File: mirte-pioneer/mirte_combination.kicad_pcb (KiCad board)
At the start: 2 copper layers, 55 x 81.9 mm, 48 parts, among them J1 Servo3, J10 IR1, J11 Conn_01x13_Female, J12 IR Object Detector 1, J14 IR2, J17 MC1, J18 MC2, J19 Servo1, J2 Conn_01x20_Female, J20 SRF1, J21 ENC2, J23 MC1-A, J24 MC1-B, J25 SRF2, J26 ENC1, J27 Servo2, J28 I2C2, J3 Servo4, J30 I2C1, J33 line out left, J34 Power in, J35 Power out, J37 on/off, J4 Conn_01x20_Female, J7 Keypad, J8 Conn_01x06_Female, J9 IR Object Detector 2, Q1 DMG2305UX, Q2 DMN2050L, SW1 on/off, U1 CH340C, U2 CH340E

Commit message: Fix logo reference name
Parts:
- renumbered G*** to G1, G*** to G2
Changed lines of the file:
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@@
     (at 112.5 58.575 -90)
     (attr board_only exclude_from_pos_files exclude_from_bom)
-    (fp_text reference "G***" (at -1.285 0.39 180) (layer "F.Fab")
+    (fp_text reference "G1" (at -1.285 0.39 180) (layer "F.Fab")
         (effects (font (size 1.524 1.524) (thickness 0.3)))
     )
@@
     (at 104.275 114.325 -90)
     (attr board_only exclude_from_pos_files exclude_from_bom)
-    (fp_text reference "G***" (at 0.425 0.75 90) (layer "F.Fab")
+    (fp_text reference "G2" (at 0.425 0.75 90) (layer "F.Fab")
         (effects (font (size 1.524 1.524) (thickness 0.3)))
     )

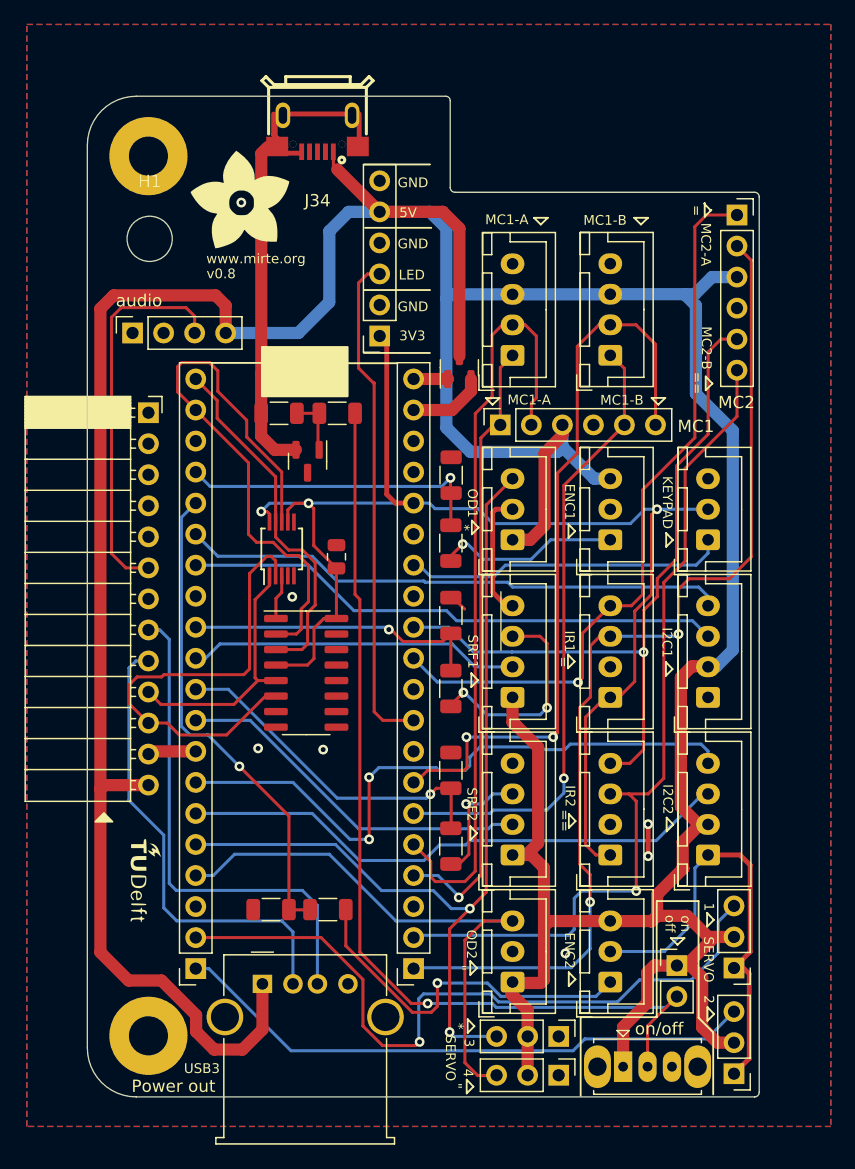
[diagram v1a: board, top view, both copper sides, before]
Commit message: Fix text unreadable servo 1&2 by move edge
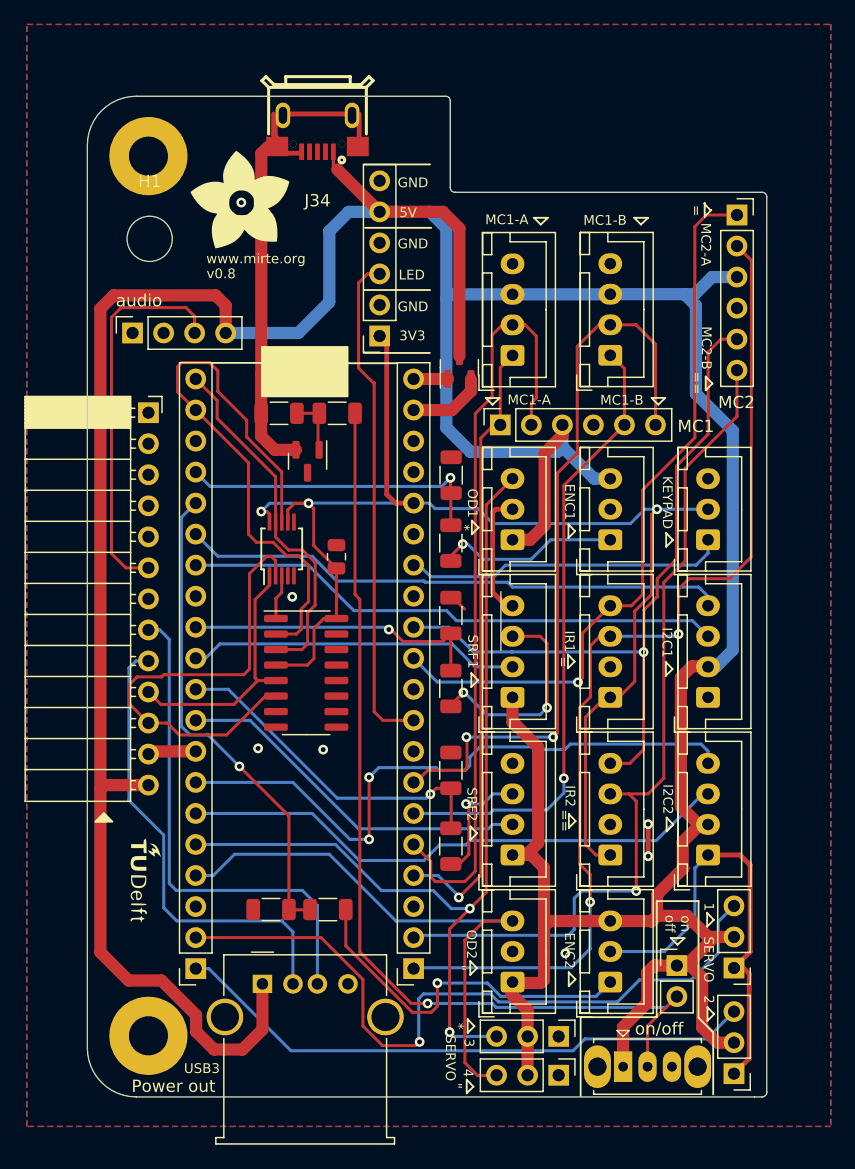
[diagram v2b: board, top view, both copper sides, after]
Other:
- board size 55 x 81.9 mm -> 55.6 x 81.9 mm
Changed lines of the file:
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@@
   (gr_line (start 104 50.1) (end 129.337 50.100408)
     (stroke (width 0.1) (type solid)) (layer "Edge.Cuts"))
-  (gr_arc (start 154.61 57.959) (mid 154.879408 58.070592) (end 154.991 58.34)
+  (gr_arc (start 155.230592 57.959) (mid 155.5 58.070592) (end 155.611592 58.34)
     (stroke (width 0.1) (type solid)) (layer "Edge.Cuts"))
   (gr_line (start 129.702592 50.466) (end 129.7 57.578)
     (stroke (width 0.1) (type solid)) (layer "Edge.Cuts"))
-  (gr_line (start 154.991 58.34) (end 154.991 131.619)
+  (gr_line (start 130.099 57.959) (end 155.230592 57.959)
+    (stroke (width 0.1) (type default)) (layer "Edge.Cuts"))
+  (gr_line (start 155.611592 58.34) (end 155.611592 131.619)
     (stroke (width 0.1) (type solid)) (layer "Edge.Cuts"))
-  (gr_arc (start 154.991 131.619) (mid 154.879408 131.888408) (end 154.61 132)
+  (gr_arc (start 155.611592 131.619) (mid 155.5 131.888408) (end 155.230592 132)
     (stroke (width 0.1) (type solid)) (layer "Edge.Cuts"))
   (gr_arc (start 129.337 50.100408) (mid 129.595513 50.207487) (end 129.702592 50.466)
     (stroke (width 0.1) (type solid)) (layer "Edge.Cuts"))
+  (gr_line (start 155.230592 132) (end 154.61 132)
+    (stroke (width 0.1) (type default)) (layer "Edge.Cuts"))
   (gr_line (start 100 128) (end 100 54.1)
     (stroke (width 0.1) (type solid)) (layer "Edge.Cuts"))
-  (gr_line (start 154.61 57.959) (end 130.099 57.959)
-    (stroke (width 0.1) (type solid)) (layer "Edge.Cuts"))
   (gr_arc (start 130.099 57.959) (mid 129.820592 57.851136) (end 129.7 57.578)

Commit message: Change obj detector to 5V, add header for usb (lego)
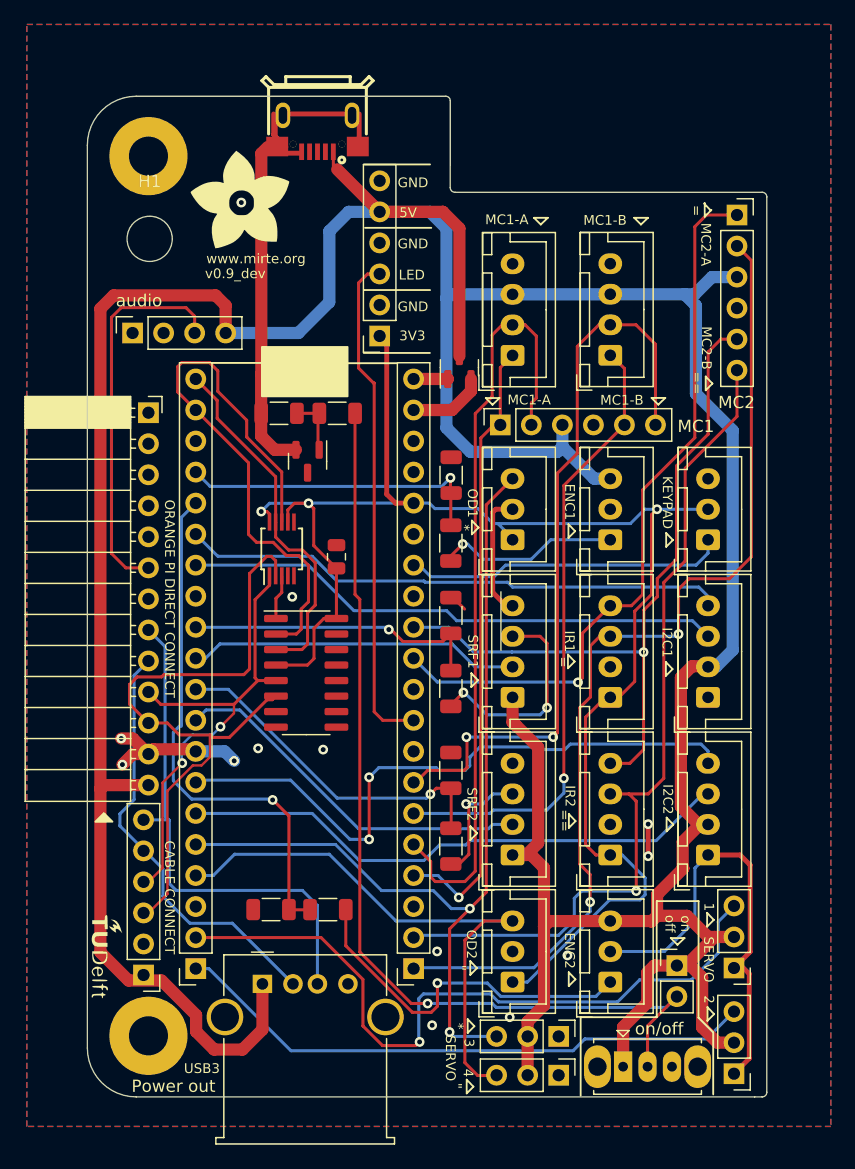
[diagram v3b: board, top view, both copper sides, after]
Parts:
- added J5: Conn_01x06_Pin, Connector_PinHeader_2.54mm:PinHeader_1x06_P2.54mm_Vertical, F.Cu at (104.6, 122.0)
- moved G2 6.99 mm to (101.1, 120.5)
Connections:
- J12 pad 1: 5V -> 3V3
- J9 pad 1: 5V -> 3V3
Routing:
- net 3V3: track 109.4 -> 130.0 mm
- net D+: track 20.8 -> 40.4 mm, vias 0 -> 2
- net D-: track 38.2 -> 56.6 mm
- net 5V: track 351.1 -> 336.6 mm
- net D_GND: track 60.3 -> 69.2 mm, vias 7 -> 13
- net GP3: track 40.0 -> 43.7 mm
- net usb-dp3: track 41.3 -> 43.6 mm
- net usb-dm3: track 38.3 -> 36.5 mm
- net GP16: track 84.9 -> 83.1 mm
- net GP9: track 29.7 -> 30.5 mm
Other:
- board text added: "CABLE CONNECT"
- board text added: "ORANGE PI DIRECT CONNECT"
- board text added: "v0.9_dev"
- board text removed: "v0.8"

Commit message: update version8, uart, usb c, usb switch
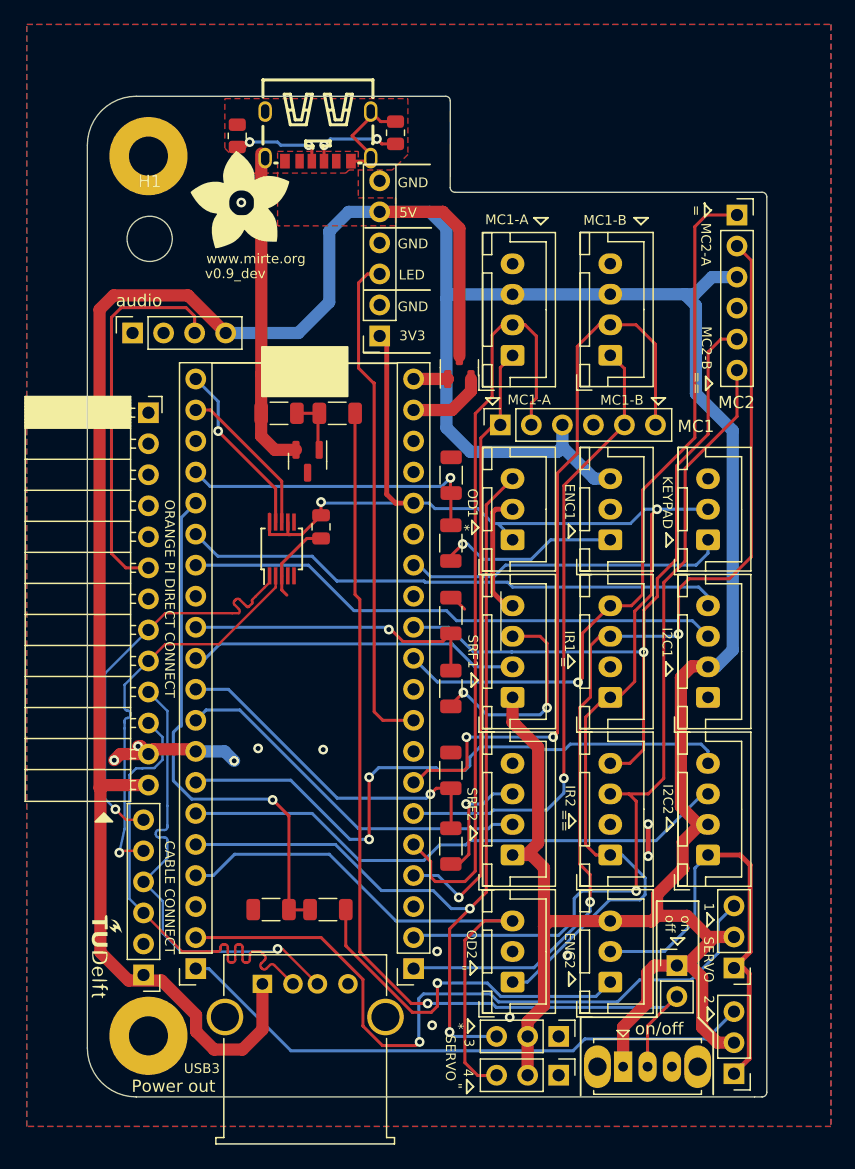
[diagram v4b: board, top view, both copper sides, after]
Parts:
- removed J34: Power in, lcsc:MICRO-USB-SMD_U254-051T-4BH83-S1S
- removed U1: CH340C, Package_SO:SOIC-16_3.9x9.9mm_P1.27mm
- added R1: 5k1, Resistor_SMD:R_0805_2012Metric, F.Cu at (125.2, 53.1)
- added R12: 5k1, Resistor_SMD:R_0805_2012Metric, F.Cu at (112.3, 53.3)
- added USB1: TYPE-C 6P(073), lcsc:TYPE-C-SMD_TYPE-C-6P_5, F.Cu at (118.9, 53.4)
- moved C1 2.75 mm to (119.1, 85.3), turned to 90 degrees
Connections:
- J11 pad 10: D+ -> usb-d2+
- J11 pad 11: D- -> usb-d2-
- J11 pad 8: usb-dp3 -> D+
- J11 pad 9: usb-dm3 -> D-
- J35 pad 2: usb-dm3 -> usb-d2-
- J35 pad 3: usb-dp3 -> usb-d2+
- J5 pad 3: D- -> usb-d2-
- J5 pad 4: D+ -> usb-d2+
- J5 pad 5: usb-dm3 -> D-
- J5 pad 6: usb-dp3 -> D+
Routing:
- net usb-dp3: track 43.6 -> 0.00 mm
- net usb-d2-: track 0.00 -> 39.3 mm
- net usb-d2+: track 0.00 -> 37.9 mm, vias 0 -> 1
- net usb-dm3: track 36.5 -> 0.00 mm
- net GP1: track 48.0 -> 12.8 mm
- net D-: track 56.6 -> 33.0 mm, vias 0 -> 1
- net 3V3: track 130.0 -> 111.0 mm, vias 3 -> 2
- net GP0: track 29.4 -> 14.4 mm, vias 0 -> 1
- net 5V: track 336.6 -> 328.8 mm
- net Net-(USB1-CC2): track 0.00 -> 7.53 mm, vias 0 -> 2
- net Net-(USB1-CC1): track 0.00 -> 7.53 mm, vias 0 -> 2
- net D+: track 40.4 -> 33.1 mm, vias 2 -> 1
- net GND: track 42.1 -> 35.6 mm
- net D_GND: track 69.2 -> 71.2 mm, vias 13 -> 12
- added copper zone on F.Cu, net 5V
- added copper zone on F.Cu, net GND

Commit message: change switch
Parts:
- removed SW1: on/off, Button_Switch_THT:SW_Slide_1P2T_CK_OS102011MS2Q
- added SW2: SK12D07VG5, lcsc:SW-TH_SK12D07VG5, F.Cu at (145.7, 129.5)
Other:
- board text added: "▼on/off"

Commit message: rotations ok
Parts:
- moved J8 1.58 mm to (125.5, 69.7)
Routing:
- net 3V3: track 111.0 -> 119.1 mm
- net GP14: track 58.9 -> 51.3 mm
- net 5V: track 328.8 -> 335.5 mm, vias 0 -> 4
- net GND: track 35.6 -> 39.1 mm
- net D_GND: track 71.2 -> 73.2 mm, vias 12 -> 18
- net GP22: track 41.2 -> 43.0 mm
- net Net-(USB1-CC2): track 7.53 -> 8.05 mm
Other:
- board text added: "JLCJLCJLCJLC"
- board text added: "v0.9"
- board text removed: "USB3"
- board text removed: "v0.9_dev"

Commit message: styling pioneer pcb 0.9
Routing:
- net D_GND: track 73.2 -> 75.3 mm, vias 18 -> 27
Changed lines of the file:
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@@
 			(at 0 -4.7 0)
 			(layer "F.SilkS")
+			(hide yes)
 			(effects
 				(font
@@
 		(sheetfile "mirte_combination.kicad_sch")
 		(attr exclude_from_pos_files exclude_from_bom)
-		(fp_circle
-			(center 0 0)
-			(end 3.7 0)
-			(stroke
-				(width 0.15)
-				(type solid)
-			)
-			(fill none)
-			(layer "Cmts.User")
-		)
-		(fp_circle
-			(center 0 0)
-			(end 3.95 0)
-			(stroke
-				(width 0.05)
-				(type solid)
-			)
-			(fill none)
-			(layer "F.CrtYd")
-		)
 		(fp_text user "${REFERENCE}"
 			(at 0 0 0)
@@
 		)
 	)
-	(gr_text "3V3"
-		(at 125.6 83.46 0)
-		(layer "B.SilkS")
-		(effects
-			(font
-				(size 0.8 0.8)
-				(thickness 0.15)
-			)
-			(justify left mirror)
-		)
-	)
 	(gr_text "GP28"
 		(at 146.275 86.4 0)
@@
 		)
 	)
+	(gr_text "3V3"
+		(at 125.6 83.46 -0)
+		(layer "F.SilkS")
+		(effects
+			(font
+				(size 0.8 0.8)
+				(thickness 0.15)
+			)
+			(justify left)
+		)
+	)
 	(gr_text "USB"
 		(at 117.76 72.46 0)
@@
 	)
 	(segment
+		(start 119.126 86.294)
+		(end 119.126 86.995)
+		(width 0.25)
+		(layer "F.Cu")
+		(net 6)
+	)
+	(segment
 		(start 134.275 91.8)
 		(end 134.8 91.8)
@@
 	)
 	(segment
+		(start 119.126 86.995)
+		(end 120.0912 87.9602)
+		(width 0.25)
+		(layer "F.Cu")
+		(net 6)
+	)
+	(segment
 		(start 154.175 128.85)
 		(end 154.175 121.925)
@@
 	)
 	(via
+		(at 113.7158 83.2866)
+		(size 0.8)
+		(drill 0.4)
+		(layers "F.Cu" "B.Cu")
+		(free yes)
+		(net 6)
+	)
+	(via
 		(at 113.975 103.475)
 		(size 0.8)
@@
 	)
 	(via
+		(at 119.0752 114.173)
+		(size 0.8)
+		(drill 0.4)
+		(layers "F.Cu" "B.Cu")
+		(free yes)
+		(net 6)
+	)
+	(via
+		(at 112.2934 74.4474)
+		(size 0.8)
+		(drill 0.4)
+		(layers "F.Cu" "B.Cu")
+		(free yes)
+		(net 6)
+	)
+	(via
 		(at 119.3 103.575)
 		(size 0.8)
@@
 	)
 	(via
+		(at 113.7158 114.046)
+		(size 0.8)
+		(drill 0.4)
+		(layers "F.Cu" "B.Cu")
+		(free yes)
+		(net 6)
+	)
+	(via
 		(at 145.9 109.675)
 		(size 0.8)
@@
 	)
 	(via
+		(at 116.2304 80.4926)
+		(size 0.8)
+		(drill 0.4)
+		(layers "F.Cu" "B.Cu")
+		(free yes)
+		(net 6)
+	)
+	(via
+		(at 111.887 84.8106)
+		(size 0.8)
+		(drill 0.4)
+		(layers "F.Cu" "B.Cu")
+		(free yes)
+		(net 6)
+	)
+	(via
 		(at 128.6256 120.0912)
 		(size 0.8)
@@
 	)
 	(via
+		(at 120.0912 87.9602)
+		(size 0.8)
+		(drill 0.4)
+		(layers "F.Cu" "B.Cu")
+		(net 6)
+	)
+	(via
 		(at 120 101.25)
 		(size 0.8)
@@
 		(size 0.8)
 		(drill 0.4)
+		(layers "F.Cu" "B.Cu")
+		(free yes)
+		(net 6)
+	)
+	(via
+		(at 121.285 79.883)
+		(size 0.8)
+		(drill 0.4)
+		(layers "F.Cu" "B.Cu")
+		(free yes)
+		(net 6)
+	)
+	(via
+		(at 120.0404 69.6214)
+		(size 0.8)
+		(drill 0.4)
